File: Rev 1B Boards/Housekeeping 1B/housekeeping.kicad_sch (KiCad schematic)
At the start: 44 parts, among them U1 MC34063A, U2 MC34063A, U3 TPS54302

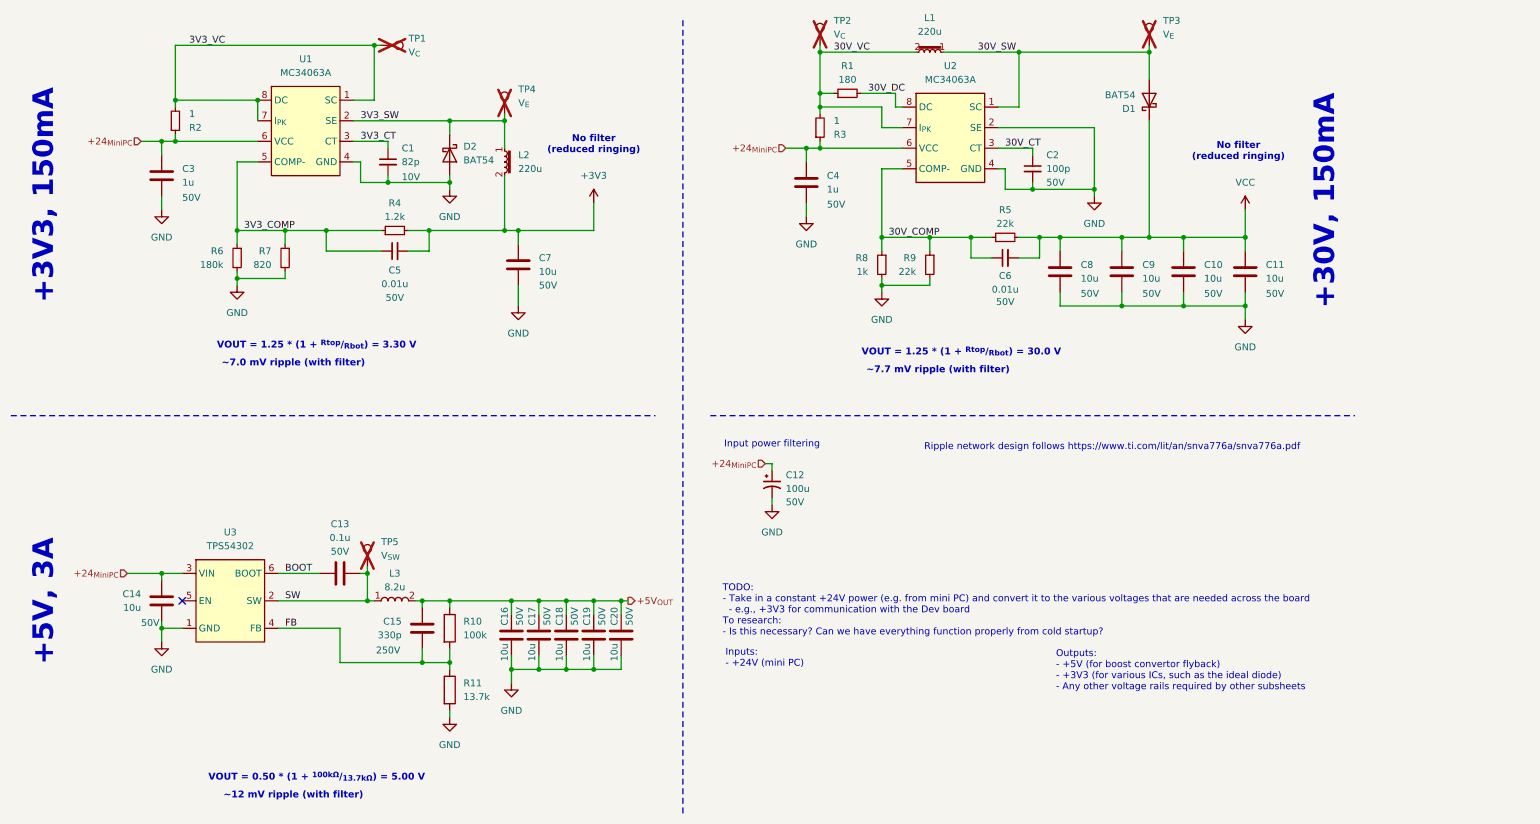
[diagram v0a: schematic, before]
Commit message: Create Housekeeping power supply test board
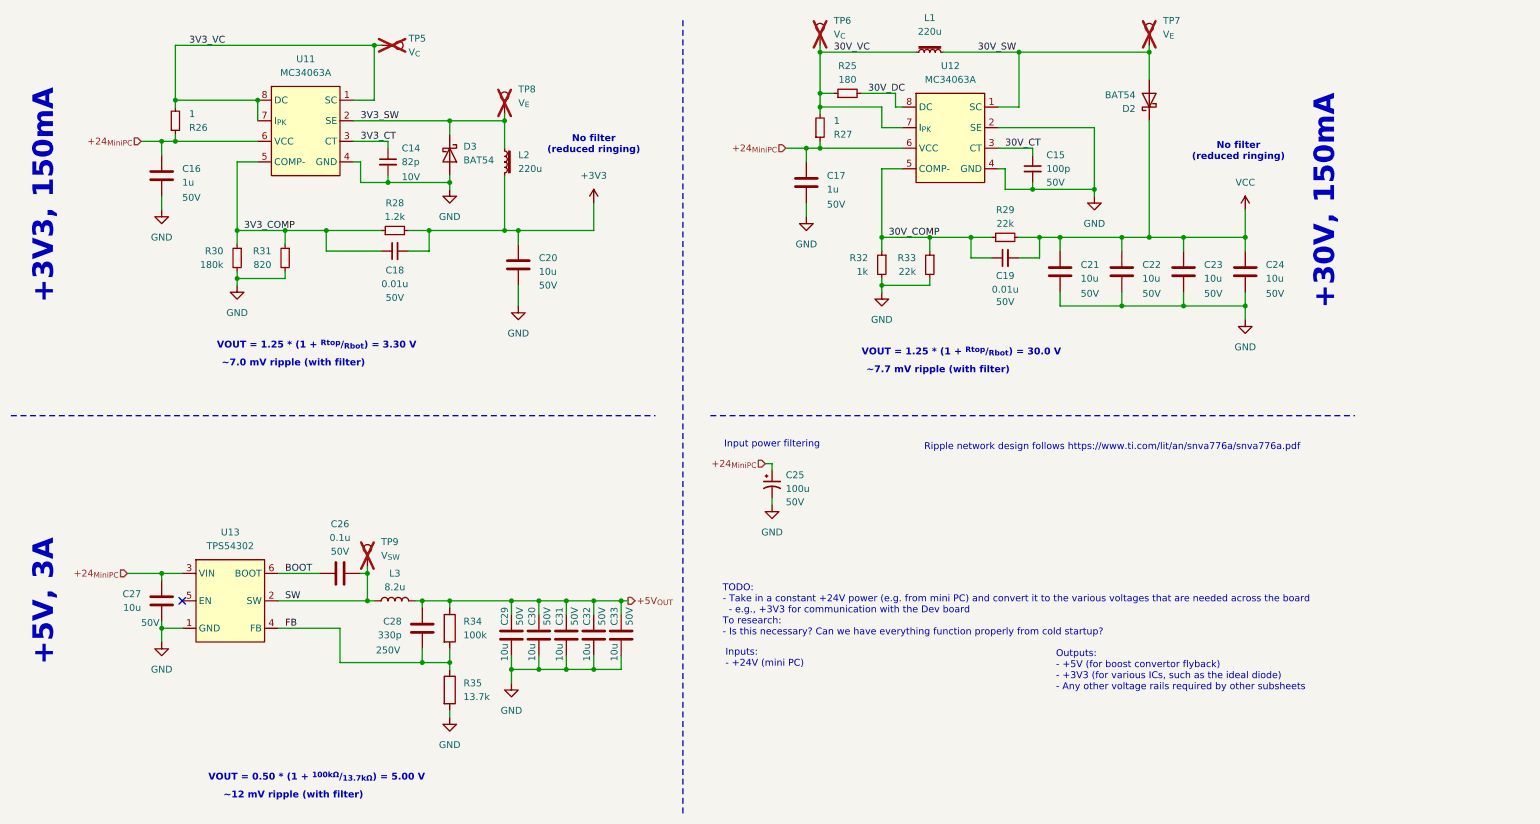
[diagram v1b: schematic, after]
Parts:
- TP7: renamed from TP3; footprint TestPoint:TestPoint_Pad_1.0x1.0mm -> TestPoint:TestPoint_Bridge_Pitch2.0mm_Drill0.7mm
- TP8: renamed from TP4; footprint TestPoint:TestPoint_Pad_1.0x1.0mm -> TestPoint:TestPoint_Bridge_Pitch2.0mm_Drill0.7mm
- renumbered C1 to C14, C2 to C15, C3 to C16, C4 to C17, C5 to C18, C6 to C19, C7 to C20, C8 to C21, C9 to C22, C10 to C23, C11 to C24, C12 to C25, C13 to C26, C14 to C27, C15 to C28, C16 to C29, C17 to C30, C18 to C31, C19 to C32, C20 to C33, D1 to D2, D2 to D3, R1 to R25, R2 to R26, R3 to R27, R4 to R28, R5 to R29, R6 to R30, R7 to R31, R8 to R32, R9 to R33, R10 to R34, R11 to R35, TP1 to TP5, TP2 to TP6, TP5 to TP9, U1 to U11, U2 to U12, U3 to U13
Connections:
- net 30V_SW: now also L1.2; no longer L1.1
- net 30V_VC: now also L1.1; no longer L1.2
